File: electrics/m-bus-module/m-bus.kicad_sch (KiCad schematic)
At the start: 35 parts, among them Q1 BC856B-13-F, Q2 BC846B-7-F, Q3 FDN5618P, U3 VOM452T, U4 VOM452T, U5 MC33072ADR2G, U6 LM4040DIM3-5.0/NOPB

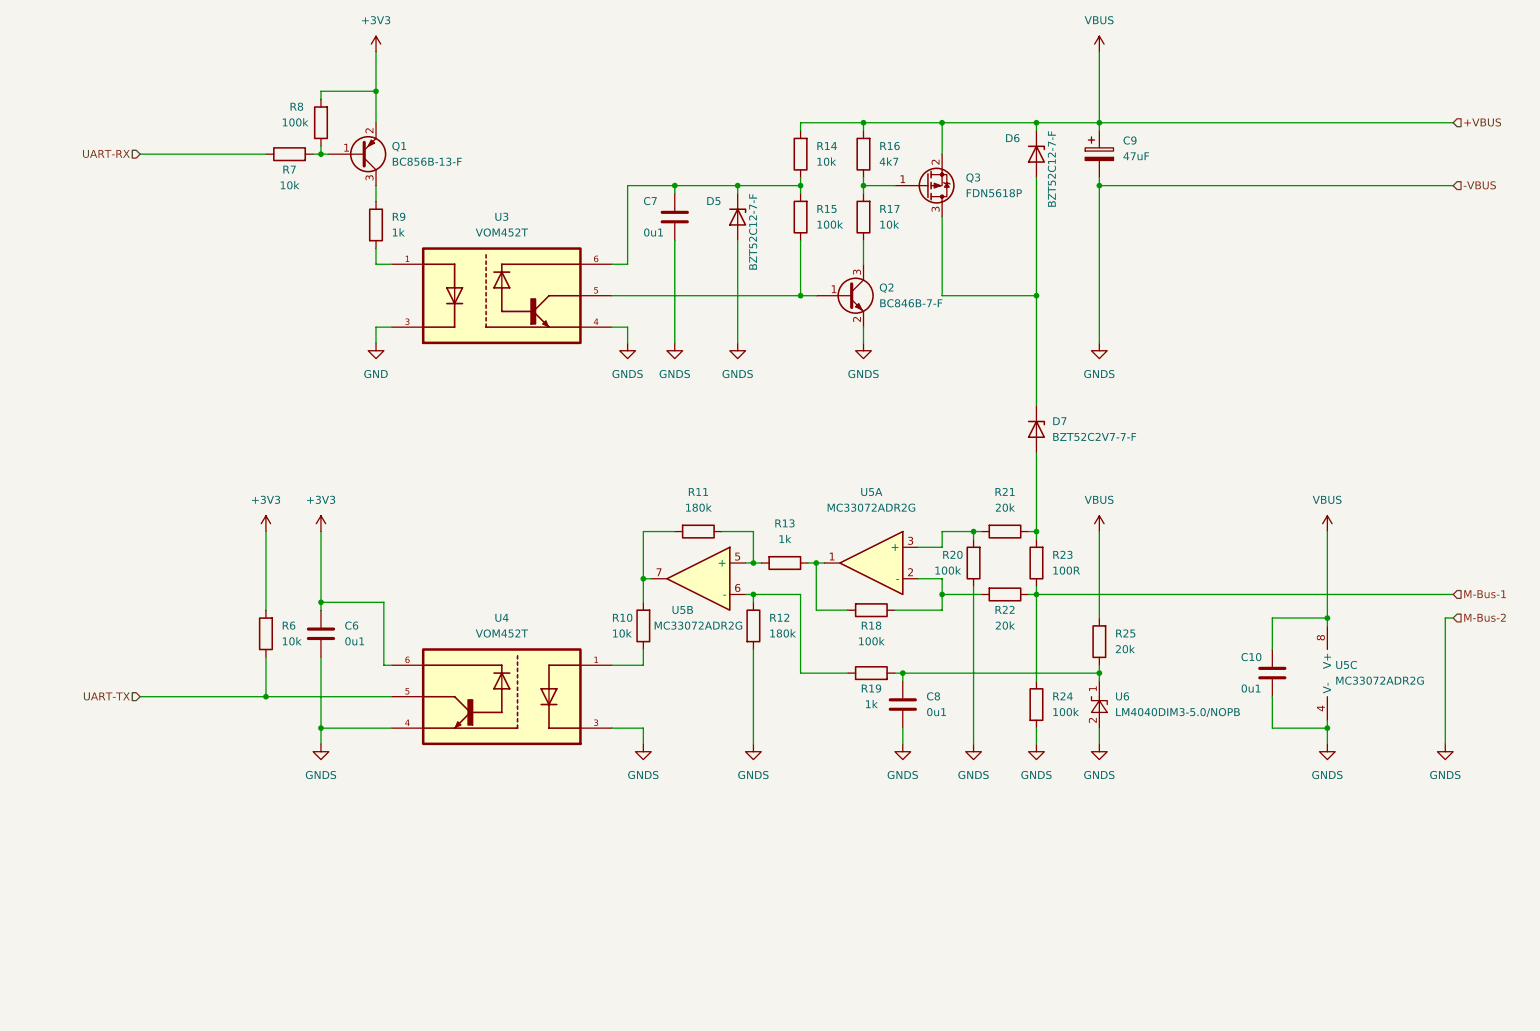
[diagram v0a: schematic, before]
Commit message: Fix all ERC and DRC warnings during build
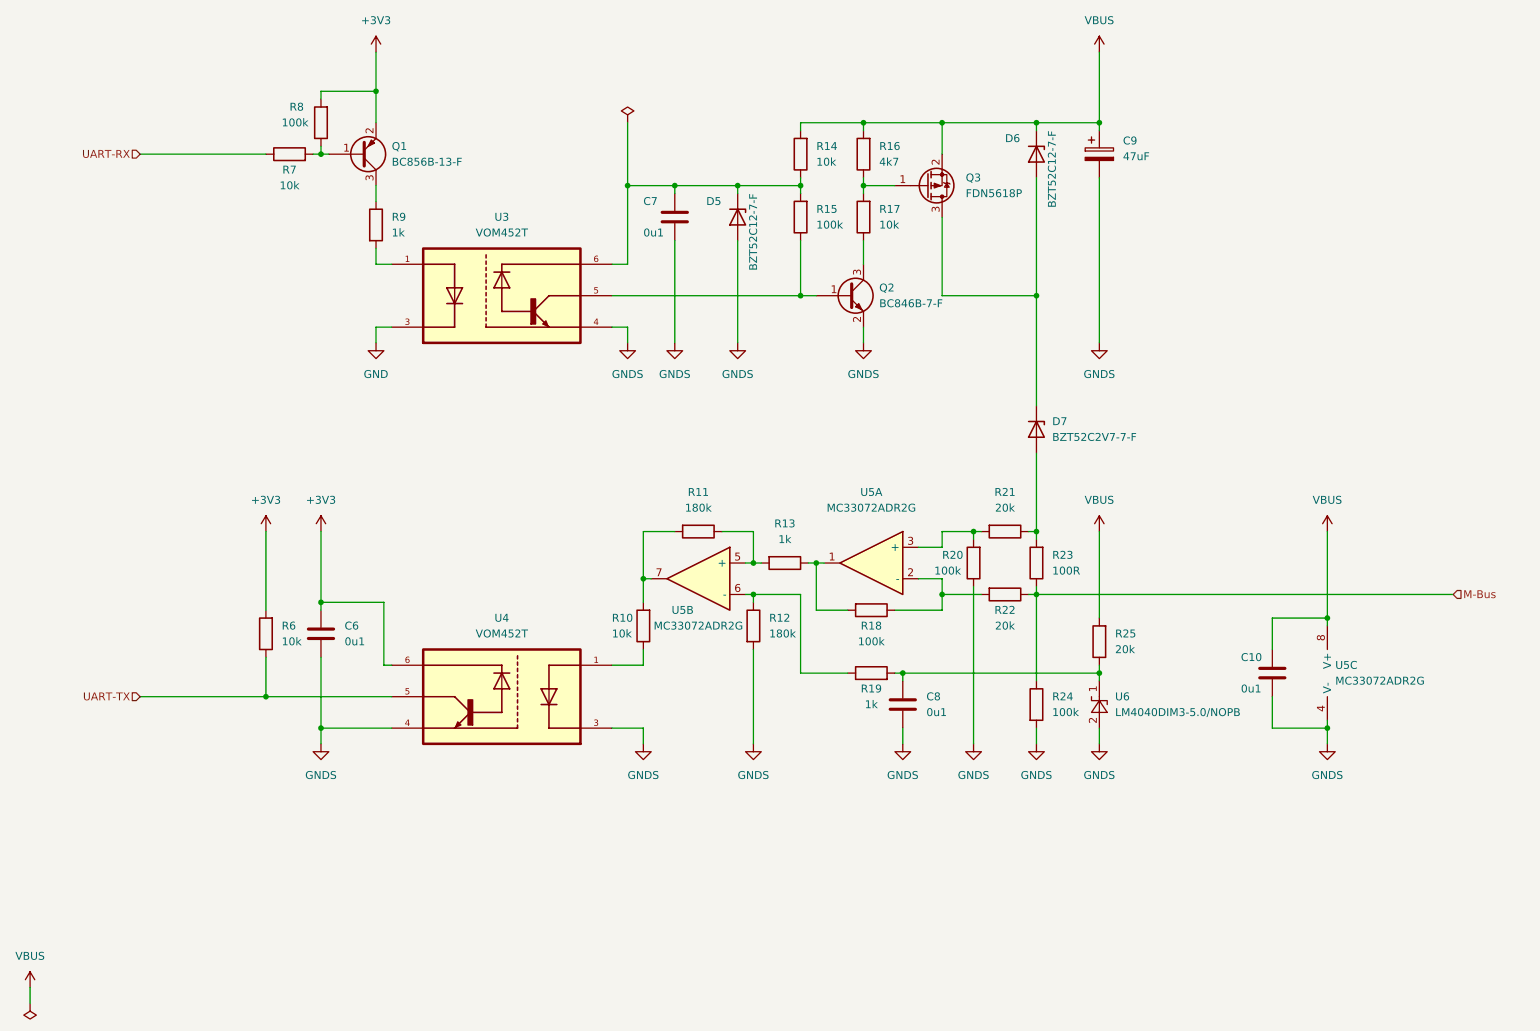
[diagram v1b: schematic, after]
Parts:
- C10, C6, C7, C8: manf# C1206C104M6RACTU -> C0603C104M4RACTU; mouser# 80-C1206C104M6R -> 80-C0603C104M4R
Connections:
- net M-Bus-1 renamed M-Bus
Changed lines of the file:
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@@
   (junction (at 142.24 114.3) (diameter 0) (color 0 0 0 0)
   )
-  (junction (at 198.12 53.34) (diameter 0) (color 0 0 0 0)
+  (junction (at 121.92 53.34) (diameter 0) (color 0 0 0 0)
   )
   (junction (at 152.4 114.3) (diameter 0) (color 0 0 0 0)
@@
     (stroke (width 0) (type default) (color 0 0 0 0))
   )
-  (wire (pts (xy 198.12 53.34) (xy 255.27 53.34))
-    (stroke (width 0) (type default) (color 0 0 0 0))
-  )
   (wire (pts (xy 172.72 116.84) (xy 172.72 119.38))
     (stroke (width 0) (type default) (color 0 0 0 0))
@@
     (stroke (width 0) (type default) (color 0 0 0 0))
   )
+  (wire (pts (xy 121.92 43.18) (xy 121.92 53.34))
+    (stroke (width 0) (type default) (color 0 0 0 0))
+  )
   (wire (pts (xy 187.96 43.18) (xy 198.12 43.18))
     (stroke (width 0) (type default) (color 0 0 0 0))
@@
     (stroke (width 0) (type default) (color 0 0 0 0))
   )
-  (wire (pts (xy 255.27 43.18) (xy 198.12 43.18))
-    (stroke (width 0) (type default) (color 0 0 0 0))
-  )
   (wire (pts (xy 226.06 128.27) (xy 226.06 123.19))
     (stroke (width 0) (type default) (color 0 0 0 0))
@@
     (stroke (width 0) (type default) (color 0 0 0 0))
   )
-  (wire (pts (xy 254 123.19) (xy 254 143.51))
-    (stroke (width 0) (type default) (color 0 0 0 0))
-  )
   (wire (pts (xy 137.16 109.22) (xy 142.24 109.22))
     (stroke (width 0) (type default) (color 0 0 0 0))
@@
     (stroke (width 0) (type default) (color 0 0 0 0))
   )
-  (wire (pts (xy 198.12 52.07) (xy 198.12 53.34))
+  (wire (pts (xy 198.12 52.07) (xy 198.12 78.74))
     (stroke (width 0) (type default) (color 0 0 0 0))
   )
@@
     (stroke (width 0) (type default) (color 0 0 0 0))
   )
+  (wire (pts (xy 25.4 182.88) (xy 25.4 185.42))
+    (stroke (width 0) (type default) (color 0 0 0 0))
+  )
   (wire (pts (xy 119.38 130.81) (xy 124.46 130.81))
     (stroke (width 0) (type default) (color 0 0 0 0))
@@
     (stroke (width 0) (type default) (color 0 0 0 0))
   )
-  (wire (pts (xy 255.27 123.19) (xy 254 123.19))
-    (stroke (width 0) (type default) (color 0 0 0 0))
-  )
   (wire (pts (xy 72.39 140.97) (xy 72.39 143.51))
     (stroke (width 0) (type default) (color 0 0 0 0))
@@
     (stroke (width 0) (type default) (color 0 0 0 0))
   )
-  (wire (pts (xy 198.12 53.34) (xy 198.12 78.74))
-    (stroke (width 0) (type default) (color 0 0 0 0))
-  )
   (wire (pts (xy 149.86 43.18) (xy 160.02 43.18))
     (stroke (width 0) (type default) (color 0 0 0 0))
@@
     (stroke (width 0) (type default) (color 0 0 0 0))
   )
-  (hierarchical_label "M-Bus-1" (shape input) (at 255.27 119.38 0)
+  (hierarchical_label "M-Bus" (shape input) (at 255.27 119.38 0)
     (effects (font (size 1.27 1.27)) (justify left))
   )
@@
     (effects (font (size 1.27 1.27)) (justify right))
   )
-  (hierarchical_label "M-Bus-2" (shape input) (at 255.27 123.19 0)
-    (effects (font (size 1.27 1.27)) (justify left))
-  )
-  (hierarchical_label "-VBUS" (shape input) (at 255.27 53.34 0)
-    (effects (font (size 1.27 1.27)) (justify left))
-  )
-  (hierarchical_label "+VBUS" (shape input) (at 255.27 43.18 0)
-    (effects (font (size 1.27 1.27)) (justify left))
-  )
   (symbol (lib_id "power:GNDS") (at 166.37 143.51 0) (unit 1)
     (in_bom yes) (on_board yes) (fields_autoplaced)
@@
     )
     (property "Datasheet" "" (id 3) (at 166.37 143.51 0)
+      (effects (font (size 1.27 1.27)) hide)
+    )
+    (pin "1")
+  )
+  (symbol (lib_id "power:VBUS") (at 25.4 182.88 0) (unit 1)
+    (in_bom yes) (on_board yes) (fields_autoplaced)
+    (property "Reference" "#PWR0106" (id 0) (at 25.4 186.69 0)
+      (effects (font (size 1.27 1.27)) hide)
+    )
+    (property "Value" "VBUS" (id 1) (at 25.4 177.8 0))
+    (property "Footprint" "" (id 2) (at 25.4 182.88 0)
+      (effects (font (size 1.27 1.27)) hide)
+    )
+    (property "Datasheet" "" (id 3) (at 25.4 182.88 0)
       (effects (font (size 1.27 1.27)) hide)
     )
@@
       (effects (font (size 1.27 1.27)) hide)
     )
-    (property "manf#" "C1206C104M6RACTU" (id 5) (at 72.39 125.73 0)
-      (effects (font (size 1.27 1.27)) hide)
-    )
-    (property "mouser#" "80-C1206C104M6R" (id 6) (at 72.39 125.73 0)
+    (property "manf#" "C0603C104M4RACTU" (id 5) (at 72.39 125.73 0)
+      (effects (font (size 1.27 1.27)) hide)
+    )
+    (property "mouser#" "80-C0603C104M4R" (id 6) (at 72.39 125.73 0)
       (effects (font (size 1.27 1.27)) hide)
     )
@@
       (effects (font (size 1.27 1.27)) hide)
     )
-    (property "manf#" "C1206C104M6RACTU" (id 5) (at 129.54 58.42 0)
-      (effects (font (size 1.27 1.27)) hide)
-    )
-    (property "mouser#" "80-C1206C104M6R" (id 6) (at 129.54 58.42 0)
+    (property "manf#" "C0603C104M4RACTU" (id 5) (at 129.54 58.42 0)
+      (effects (font (size 1.27 1.27)) hide)
+    )
+    (property "mouser#" "80-C0603C104M4R" (id 6) (at 129.54 58.42 0)
       (effects (font (size 1.27 1.27)) hide)
     )
@@
       (effects (font (size 1.27 1.27)) hide)
     )
-    (property "manf#" "C1206C104M6RACTU" (id 5) (at 226.06 132.08 0)
-      (effects (font (size 1.27 1.27)) hide)
-    )
-    (property "mouser#" "80-C1206C104M6R" (id 6) (at 226.06 132.08 0)
+    (property "manf#" "C0603C104M4RACTU" (id 5) (at 226.06 132.08 0)
+      (effects (font (size 1.27 1.27)) hide)
+    )
+    (property "mouser#" "80-C0603C104M4R" (id 6) (at 226.06 132.08 0)
       (effects (font (size 1.27 1.27)) hide)
     )
@@
     (pin "2")
   )
-  (symbol (lib_id "power:GNDS") (at 254 143.51 0) (unit 1)
-    (in_bom yes) (on_board yes) (fields_autoplaced)
-    (property "Reference" "#PWR039" (id 0) (at 254 149.86 0)
-      (effects (font (size 1.27 1.27)) hide)
-    )
-    (property "Value" "GNDS" (id 1) (at 254 148.59 0))
-    (property "Footprint" "" (id 2) (at 254 143.51 0)
-      (effects (font (size 1.27 1.27)) hide)
-    )
-    (property "Datasheet" "" (id 3) (at 254 143.51 0)
-      (effects (font (size 1.27 1.27)) hide)
-    )
-    (pin "1")
-  )
   (symbol (lib_id "Device:R") (at 147.32 114.3 270) (unit 1)
     (in_bom yes) (on_board yes) (fields_autoplaced)
@@
     (pin "1")
     (pin "2")
+  )
+  (symbol (lib_id "power:PWR_FLAG") (at 121.92 43.18 0) (unit 1)
+    (in_bom yes) (on_board yes) (fields_autoplaced)
+    (property "Reference" "#FLG0107" (id 0) (at 121.92 41.275 0)
+      (effects (font (size 1.27 1.27)) hide)
+    )
+    (property "Value" "PWR_FLAG" (id 1) (at 121.92 38.1 0)
+      (effects (font (size 1.27 1.27)) hide)
+    )
+    (property "Footprint" "" (id 2) (at 121.92 43.18 0)
+      (effects (font (size 1.27 1.27)) hide)
+    )
+    (property "Datasheet" "~" (id 3) (at 121.92 43.18 0)
+      (effects (font (size 1.27 1.27)) hide)
+    )
+    (pin "1")
   )
   (symbol (lib_id "power:GNDS") (at 129.54 78.74 0) (unit 1)
@@
     (pin "1")
     (pin "2")
+  )
+  (symbol (lib_id "power:PWR_FLAG") (at 25.4 185.42 180) (unit 1)
+    (in_bom yes) (on_board yes) (fields_autoplaced)
+    (property "Reference" "#FLG0105" (id 0) (at 25.4 187.325 0)
+      (effects (font (size 1.27 1.27)) hide)
+    )
+    (property "Value" "PWR_FLAG" (id 1) (at 25.4 190.5 0)
+      (effects (font (size 1.27 1.27)) hide)
+    )
+    (property "Footprint" "" (id 2) (at 25.4 185.42 0)
+      (effects (font (size 1.27 1.27)) hide)
+    )
+    (property "Datasheet" "~" (id 3) (at 25.4 185.42 0)
+      (effects (font (size 1.27 1.27)) hide)
+    )
+    (pin "1")
   )
   (symbol (lib_id "Device:D_Zener") (at 187.96 92.71 270) (unit 1)
@@
       (effects (font (size 1.27 1.27)) hide)
     )
-    (property "manf#" "C1206C104M6RACTU" (id 5) (at 166.37 137.16 0)
-      (effects (font (size 1.27 1.27)) hide)
-    )
-    (property "mouser#" "80-C1206C104M6R" (id 6) (at 166.37 137.16 0)
-      (effects (font (size 1.27 1.27)) hide)
-    )
+    (property "manf#" "C0603C104M4RACTU" (id 5) (at 166.37 137.16 0)
+      (effects (font (size 1.27 1.27)) hide)
+    )
+    (property "mouser#" "80-C0603C104M4R" (id 6) (at 166.37 137.16 0)
+      (effects (font (size 1.27 1.27)) hide)
+    )
